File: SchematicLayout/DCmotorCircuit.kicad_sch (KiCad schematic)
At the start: 10 parts, among them J1 Power, J2 Digital/PWM, J3 Analog, J4 Digital/PWM, J5 MotorConnector, J6 Conn_01x01_Socket, SW1 RotaryEncoder_Switch, U1 DRV8833

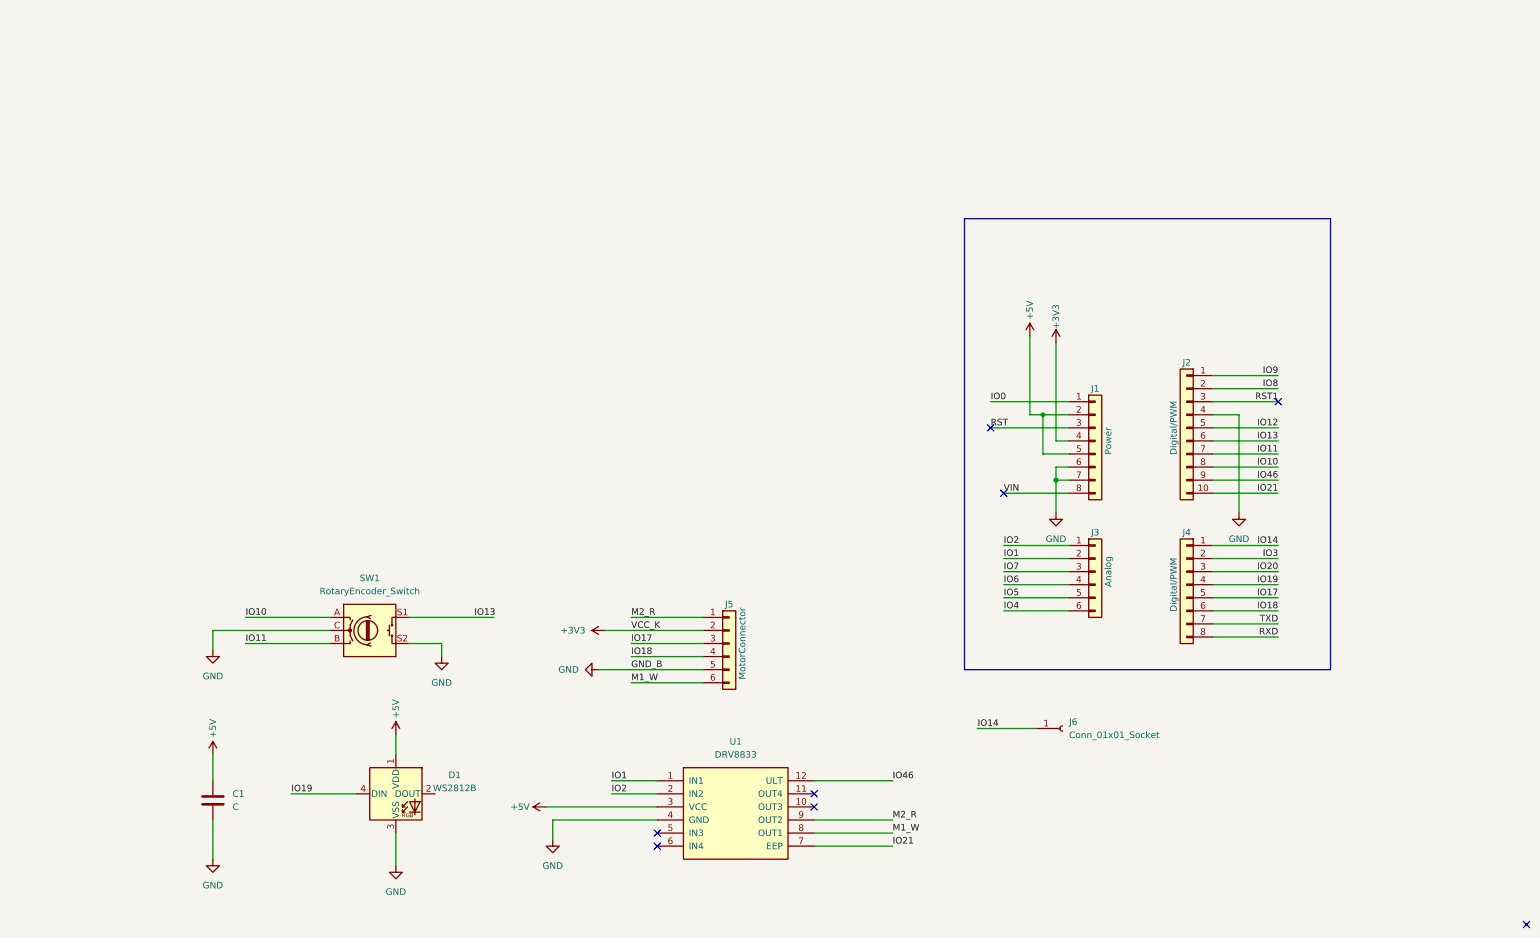
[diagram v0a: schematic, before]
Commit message: circuit updated with analog filter for the encoder GY-40
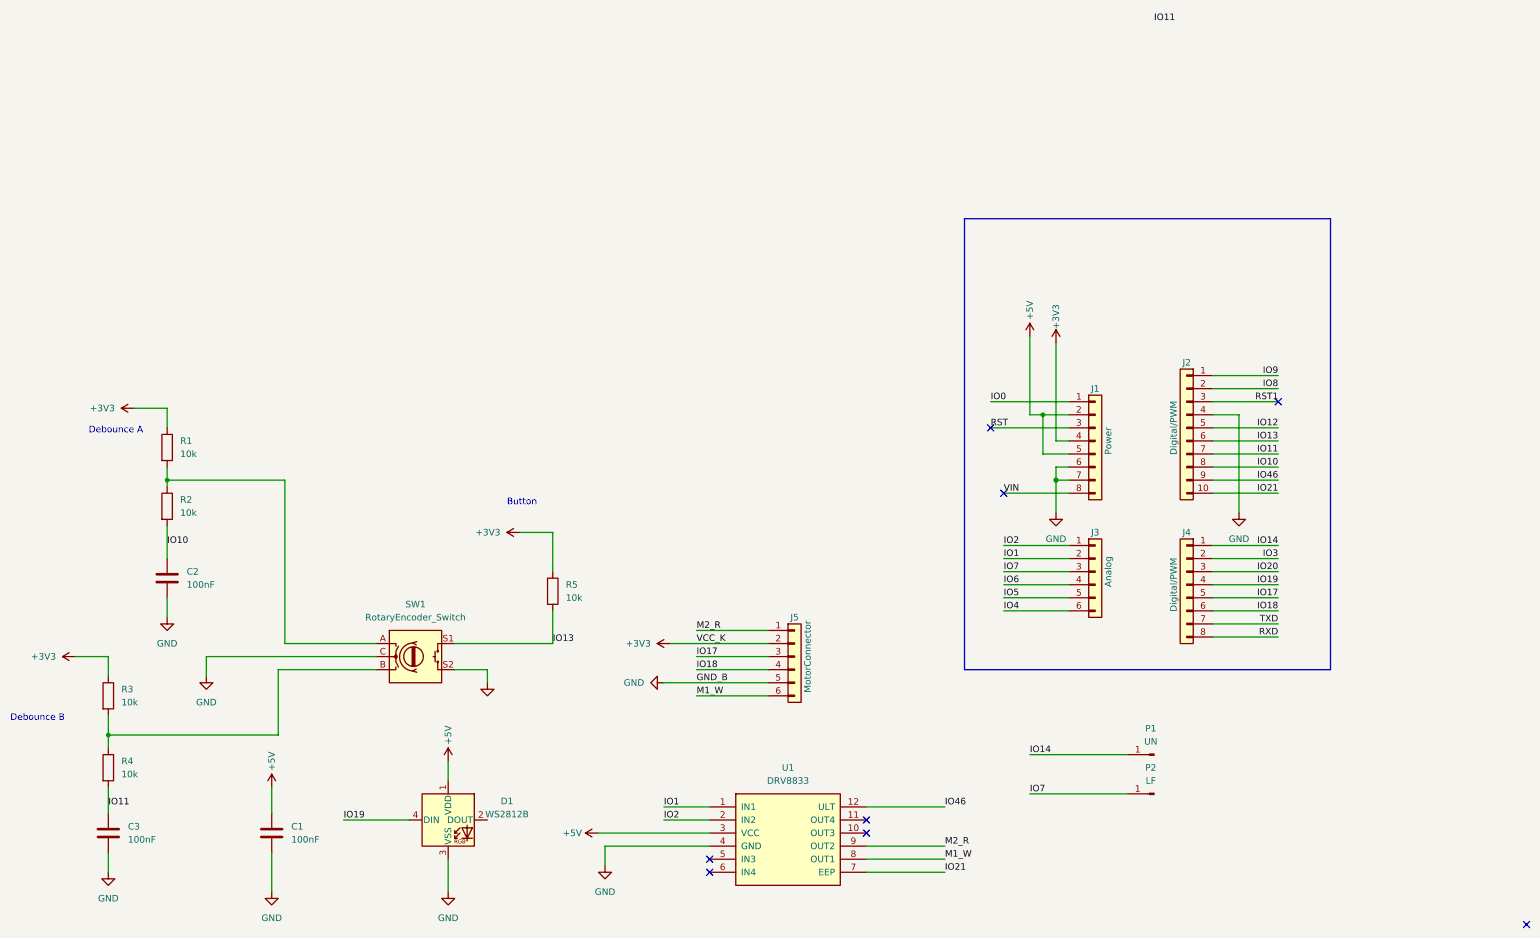
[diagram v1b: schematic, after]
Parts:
- removed J6: Conn_01x01_Socket, Connector_PinHeader_1.00mm:PinHeader_1x01_P1.00mm_Vertical, symbol Connector:Conn_01x01_Socket
- added C2, C3: 100nF, Capacitor_SMD:C_0805_2012Metric_Pad1.18x1.45mm_HandSolder, symbol Device:C
- added P1: UN, MountingHole:MountingHole_5mm_Pad_TopOnly, symbol Connector:Conn_01x01_Pin
- added P2: LF, MountingHole:MountingHole_5mm_Pad_TopOnly, symbol Connector:Conn_01x01_Pin
- added R1, R2, R3, R4, R5: 10k, Resistor_SMD:R_0805_2012Metric_Pad1.20x1.40mm_HandSolder, symbol Device:R
- C1: value C -> 100nF
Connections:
- net +3V3: now also R1.1, R3.1, R5.1
- net GND: now also C2.2, C3.2
- net IO10: now also C2.1, R2.2; no longer SW1.A
- net IO11: now also C3.1, R4.2; no longer SW1.B
- net IO13: now also R5.2
- net IO14: now also P1.1 (Pin_1)
- net IO7: now also P2.1 (Pin_1)
- new net: R3.2, R4.1, SW1.B
- new net: R1.2, R2.1, SW1.A
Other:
- note added: "Button"
- note added: "Debounce A"
- note added: "Debounce B"
- moved on the sheet: C1, D1, J5, SW1, U1
